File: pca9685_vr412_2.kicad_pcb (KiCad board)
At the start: 2 copper layers, 65 x 56 mm, 55 parts, among them J1 I2Cbus, J10 C4GND, J11 C4VDD, J12 C4VDD, J13 C4VDD, J14 C4VDD, J15 USB_B_Micro, J16 Conn_02x20, J2 Conn_01x02, J3 LED03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

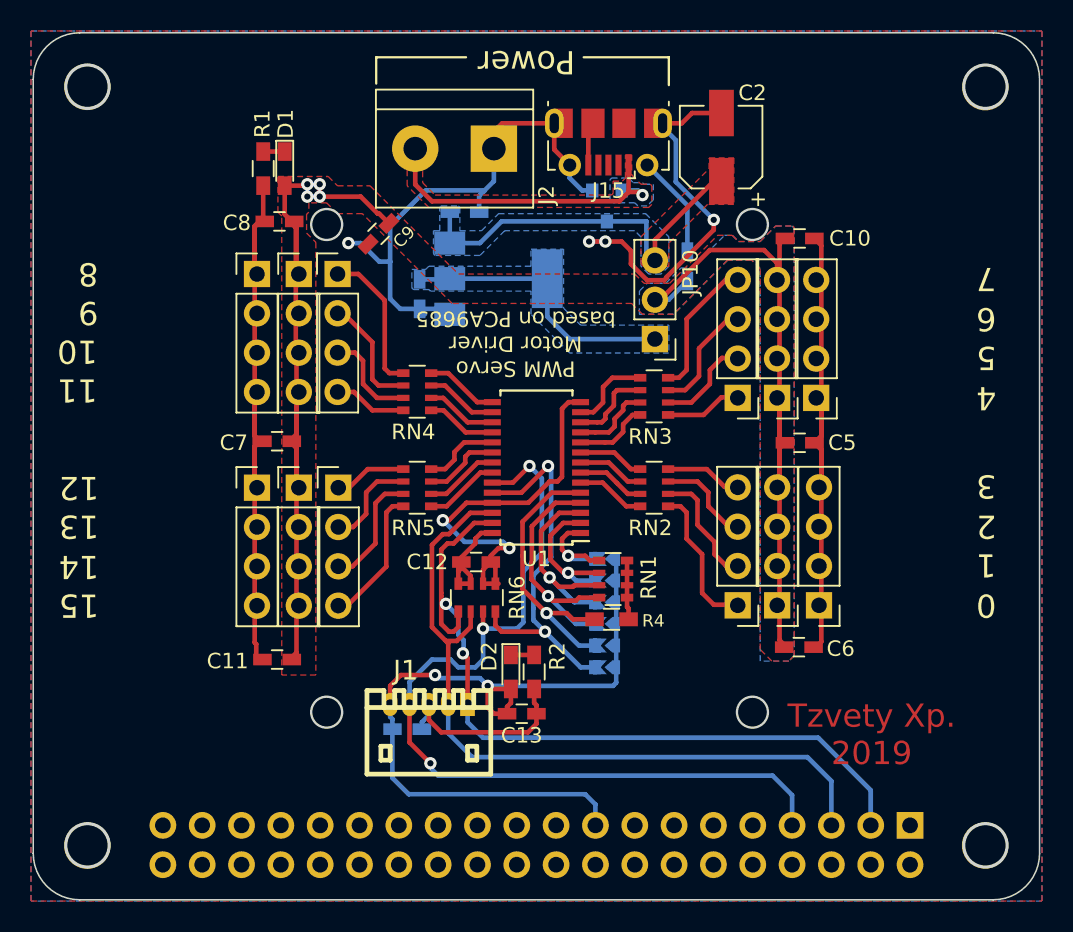
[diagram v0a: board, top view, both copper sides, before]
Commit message: Updated layout
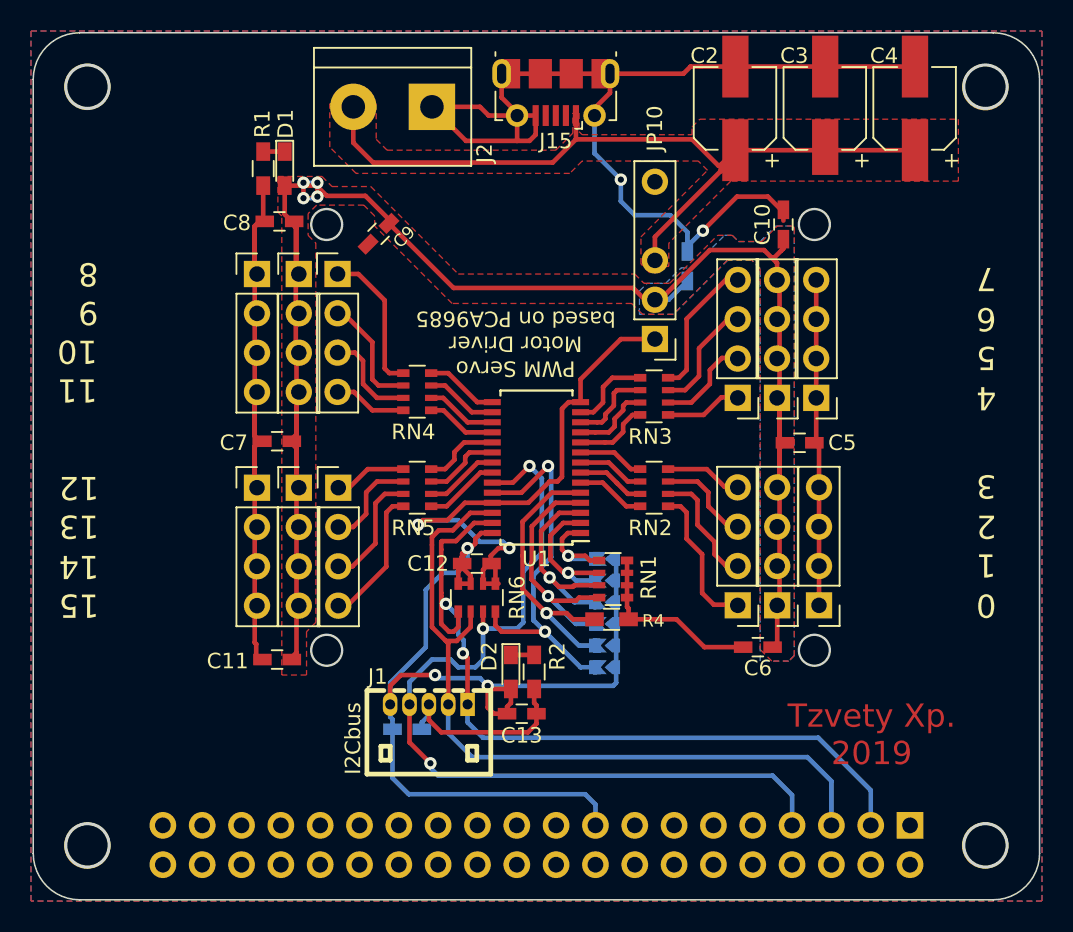
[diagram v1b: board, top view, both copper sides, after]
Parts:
- removed Q1: Q_NMOS_GDS, TO_SOT_Packages_SMD:SOT-23
- removed U2: AMS1117-5.0, TO_SOT_Packages_SMD:SOT-223-3_TabPin2
- C3, C4: value 0.1uF -> 10uF; footprint Capacitors_SMD:C_0603_HandSoldering -> Capacitors_SMD:CP_Elec_5x5.3; moved to F.Cu
- JP10: footprint Pin_Headers:Pin_Header_Straight_1x03_Pitch2.54mm -> Pin_Headers:Pin_Header_Straight_1x05_Pitch2.54mm
- moved C4 34.2 mm to (167.1, 90.8), turned to 90 degrees
- moved C3 24.2 mm to (161.3, 90.8), turned to 90 degrees
- moved J2 4.83 mm to (135.9, 90.7)
- moved J15 4.67 mm to (143.9, 89.8)
- moved C2 2.66 mm to (155.5, 90.8)
- moved C6 2.65 mm to (156.9, 125.6), turned to 180 degrees
- moved C10 1.38 mm to (158.6, 98.3), turned to 90 degrees
- moved C12 0.11 mm to (138.8, 120.2)
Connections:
- C4 pad 1: Net-(C4-Pad1) -> VCC
- J15 pad 1: Net-(J15-Pad1) -> VCC
- J2 pad 2: Net-(J15-Pad1) -> VCC
- JP10 pad 1: Net-(C4-Pad1) -> GND
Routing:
- net VCC: track 26.1 -> 52.4 mm
- net Net-(J15-Pad1): track 23.2 -> 0.00 mm, vias 1 -> 0
- net +5V: track 97.8 -> 117.6 mm
- net Net-(C4-Pad1): track 18.3 -> 0.00 mm
- net VDD: track 59.4 -> 73.3 mm, vias 2 -> 3
- net GND: track 186.2 -> 197.3 mm, vias 6 -> 4
- removed copper zone on B.Cu, net Net-(C4-Pad1)
- removed copper zone on B.Cu, net Net-(J15-Pad1)
- removed copper zone on F.Cu, net Net-(J15-Pad1)
- removed copper zone on B.Cu, net VCC
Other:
- outline, holes or cut-outs redrawn
- board text removed: "A"
- board text removed: "ERROR"
- board text removed: "Power"
